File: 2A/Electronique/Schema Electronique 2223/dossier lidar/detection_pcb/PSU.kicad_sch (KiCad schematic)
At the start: 9 parts, among them J1 BAT, Q1 PMOS, U17 Buck_3.3V

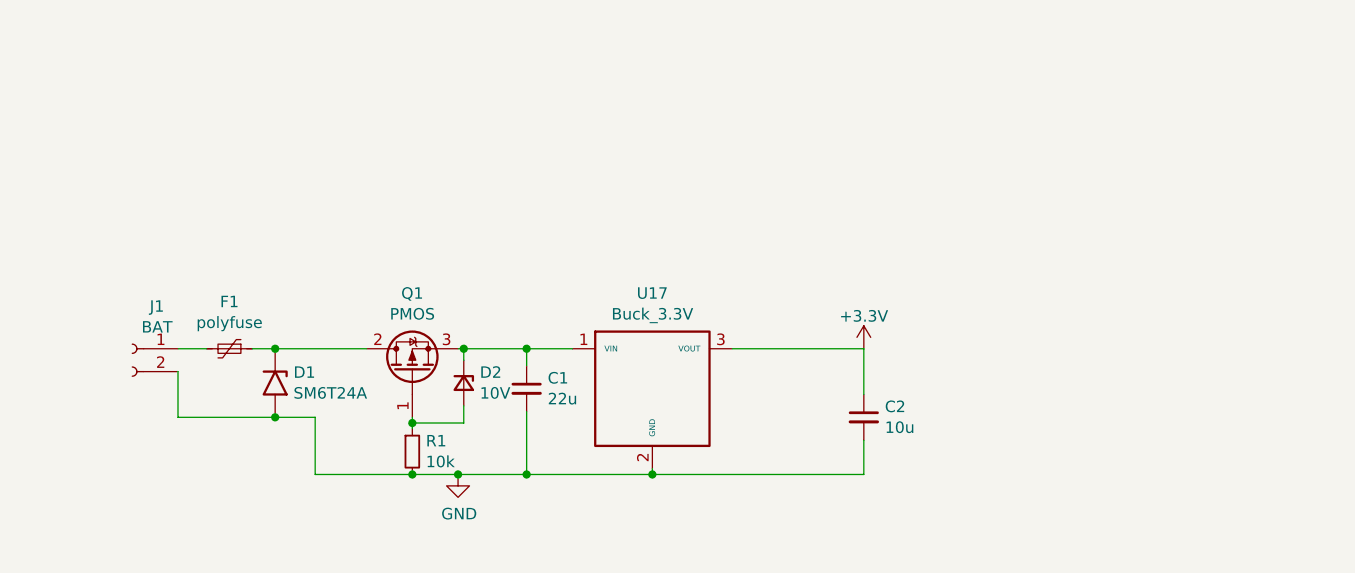
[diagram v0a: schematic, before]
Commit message: removed duplicated project, updated schematic and pcb, added BOM
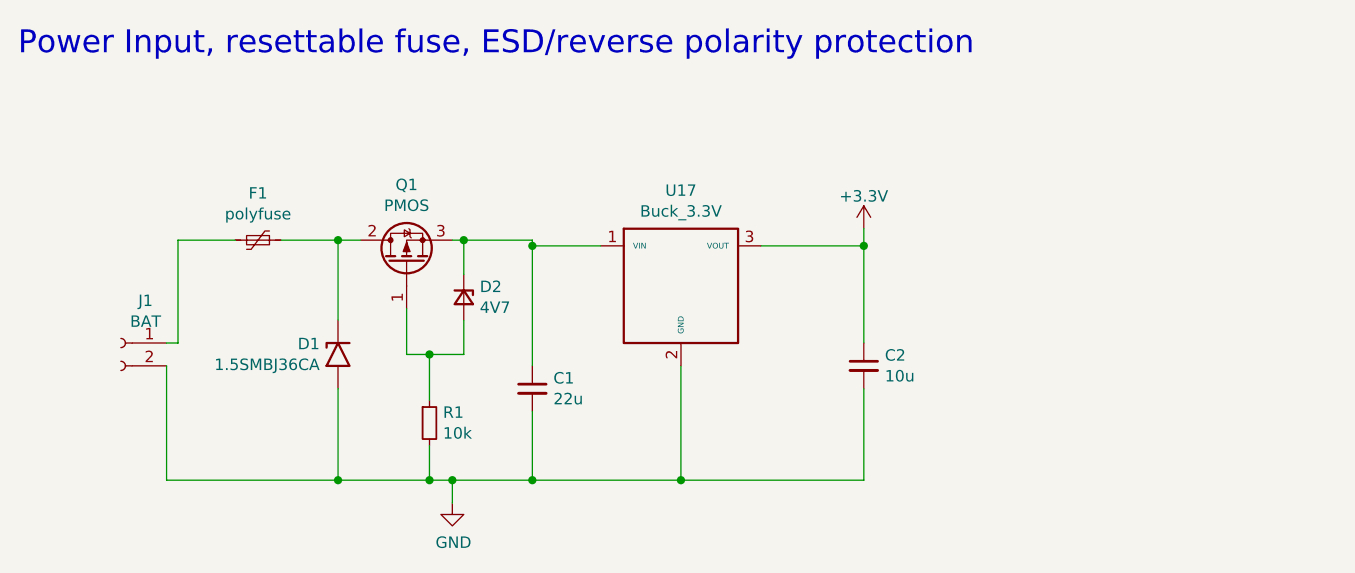
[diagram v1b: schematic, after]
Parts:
- D1: value SM6T24A -> 1.5SMBJ36CA; Mouser Part Number (none) -> 652-1.5SMBJ36CA-H
- D2: value 10V -> 4V7; Mouser Part Number (none) -> 771-BZX84J-C4V7115
- F1: Mouser Part Number (none) -> 576-1812L050/60MR
- Q1: Mouser Part Number (none) -> 78-SI2371EDS-T1-BE3
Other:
- note added: "Power Input, resettable fuse, ESD/reverse polarity protection"
- moved on the sheet: C1, C2, D1, D2, F1, J1, Q1, R1, U17
